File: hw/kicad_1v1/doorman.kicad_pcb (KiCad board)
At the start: 2 copper layers, 28 x 80 mm, 20 parts, among them J1 Ring Detection, J2 Lock, J3 Power Supply, K1 S1A05, Q1 BC337, U1 WeMos_mini, U2 PC817

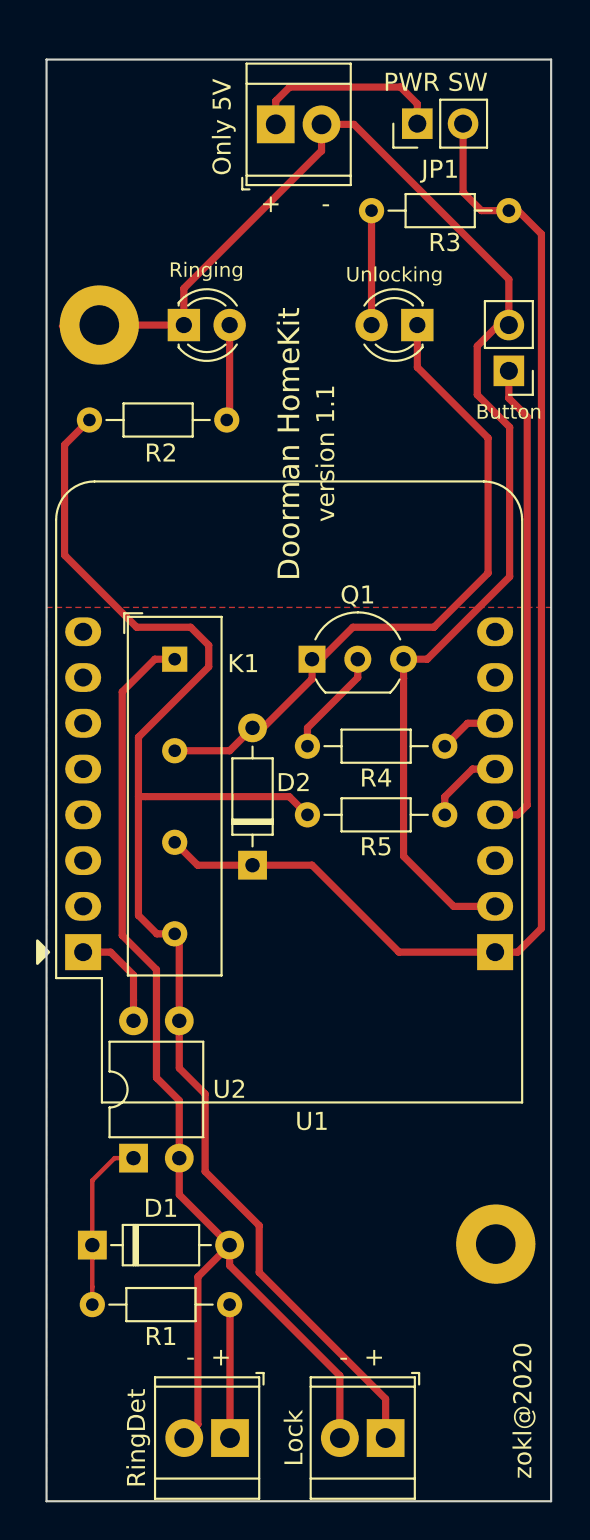
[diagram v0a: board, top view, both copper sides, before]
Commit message: Change description layout. Add cotas.
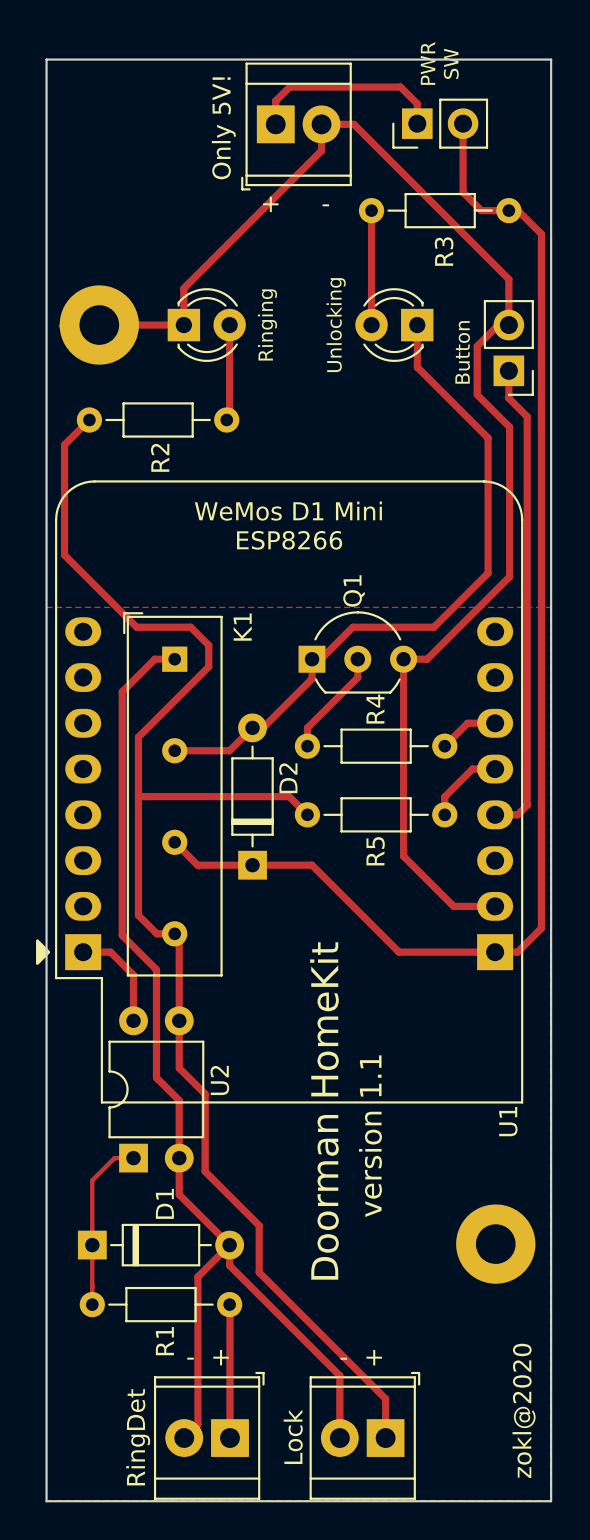
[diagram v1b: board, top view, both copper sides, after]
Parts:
-  : renamed from JP1
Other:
- board text added: "Only 5V!"
- board text added: "WeMos D1 Mini ESP8266"
- board text removed: "Only 5V"
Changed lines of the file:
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@@
   (general
     (thickness 1.6)
-    (drawings 21)
+    (drawings 24)
     (tracks 118)
     (zones 0)
@@
       (outputformat 4)
       (mirror false)
-      (drillshape 0)
+      (drillshape 2)
       (scaleselection 1)
       (outputdirectory "./"))
@@
     (descr "Through hole straight pin header, 1x02, 2.54mm pitch, single row")
     (tags "Through hole pin header THT 1x02 2.54mm single row")
-    (fp_text reference JP1 (at -2.54 1.27 180) (layer F.SilkS)
+    (fp_text reference " " (at 3.302 1.016 270) (layer F.SilkS)
       (effects (font (size 1 1) (thickness 0.15)))
     )
@@
     (descr "Diode, DO-35_SOD27 series, Axial, Horizontal, pin pitch=7.62mm, , length*diameter=4*2mm^2, , http://www.diodes.com/_files/packages/DO-35.pdf")
     (tags "Diode DO-35_SOD27 series Axial Horizontal pin pitch 7.62mm  length 4mm diameter 2mm")
-    (fp_text reference D1 (at 3.81 -2.032 -180) (layer F.SilkS)
+    (fp_text reference D1 (at 4.064 -2.286 90) (layer F.SilkS)
       (effects (font (size 1 1) (thickness 0.15)))
     )
@@
     (descr "4-lead though-hole mounted DIP package, row spacing 7.62 mm (300 mils)")
     (tags "THT DIP DIL PDIP 2.54mm 7.62mm 300mil")
-    (fp_text reference U2 (at 3.81 5.334 180) (layer F.SilkS)
+    (fp_text reference U2 (at 4.318 4.826 270) (layer F.SilkS)
       (effects (font (size 1 1) (thickness 0.15)))
     )
@@
     (descr "Resistor, Axial_DIN0204 series, Axial, Horizontal, pin pitch=7.62mm, 0.167W, length*diameter=3.6*1.6mm^2, http://cdn-reichelt.de/documents/datenblatt/B400/1_4W%23YAG.pdf")
     (tags "Resistor Axial_DIN0204 series Axial Horizontal pin pitch 7.62mm 0.167W length 3.6mm diameter 1.6mm")
-    (fp_text reference R5 (at 3.81 1.778) (layer F.SilkS)
+    (fp_text reference R5 (at 3.81 2.032 90) (layer F.SilkS)
       (effects (font (size 1 1) (thickness 0.15)))
     )
@@
     (descr "Diode, DO-35_SOD27 series, Axial, Horizontal, pin pitch=7.62mm, , length*diameter=4*2mm^2, , http://www.diodes.com/_files/packages/DO-35.pdf")
     (tags "Diode DO-35_SOD27 series Axial Horizontal pin pitch 7.62mm  length 4mm diameter 2mm")
-    (fp_text reference D2 (at 4.572 2.286 180) (layer F.SilkS)
+    (fp_text reference D2 (at 4.826 2.032 270) (layer F.SilkS)
       (effects (font (size 1 1) (thickness 0.15)))
     )
@@
     (descr "Resistor, Axial_DIN0204 series, Axial, Horizontal, pin pitch=7.62mm, 0.167W, length*diameter=3.6*1.6mm^2, http://cdn-reichelt.de/documents/datenblatt/B400/1_4W%23YAG.pdf")
     (tags "Resistor Axial_DIN0204 series Axial Horizontal pin pitch 7.62mm 0.167W length 3.6mm diameter 1.6mm")
-    (fp_text reference R4 (at 3.81 1.778) (layer F.SilkS)
+    (fp_text reference R4 (at 3.81 -2.032 90) (layer F.SilkS)
       (effects (font (size 1 1) (thickness 0.15)))
     )
@@
     (descr "16-pin module, column spacing 22.86 mm (900 mils), https://wiki.wemos.cc/products:d1:d1_mini, https://c1.staticflickr.com/1/734/31400410271_f278b087db_z.jpg")
     (tags "ESP8266 WiFi microcontroller")
-    (fp_text reference U1 (at 12.7 27.178) (layer F.SilkS)
+    (attr smd)
+    (fp_text reference U1 (at 23.622 27.178 90) (layer F.SilkS)
       (effects (font (size 1 1) (thickness 0.15)))
     )
@@
     (descr "TO-92 leads in-line, wide, drill 0.75mm (see NXP sot054_po.pdf)")
     (tags "to-92 sc-43 sc-43a sot54 PA33 transistor")
-    (fp_text reference Q1 (at 2.54 -3.556 180) (layer F.SilkS)
+    (fp_text reference Q1 (at 2.286 -3.81 270) (layer F.SilkS)
       (effects (font (size 1 1) (thickness 0.15)))
     )
@@
     (descr "Resistor, Axial_DIN0204 series, Axial, Horizontal, pin pitch=7.62mm, 0.167W, length*diameter=3.6*1.6mm^2, http://cdn-reichelt.de/documents/datenblatt/B400/1_4W%23YAG.pdf")
     (tags "Resistor Axial_DIN0204 series Axial Horizontal pin pitch 7.62mm 0.167W length 3.6mm diameter 1.6mm")
-    (fp_text reference R2 (at 3.65 -1.844) (layer F.SilkS)
+    (fp_text reference R2 (at 3.65 -2.098 90) (layer F.SilkS)
       (effects (font (size 1 1) (thickness 0.15)))
     )
@@
     (descr "Standex-Meder SIL-relais, Form 1A, see https://standexelectronics.com/wp-content/uploads/datasheet_reed_relay_SIL.pdf")
     (tags "Standex Meder SIL reed relais")
-    (fp_text reference K1 (at 0.254 -3.81 180) (layer F.SilkS)
+    (fp_text reference K1 (at -1.778 -3.81 270) (layer F.SilkS)
       (effects (font (size 1 1) (thickness 0.15)))
     )
@@
     (descr "Resistor, Axial_DIN0204 series, Axial, Horizontal, pin pitch=7.62mm, 0.167W, length*diameter=3.6*1.6mm^2, http://cdn-reichelt.de/documents/datenblatt/B400/1_4W%23YAG.pdf")
     (tags "Resistor Axial_DIN0204 series Axial Horizontal pin pitch 7.62mm 0.167W length 3.6mm diameter 1.6mm")
-    (fp_text reference R3 (at 4.064 1.778) (layer F.SilkS)
+    (fp_text reference R3 (at 4.064 2.286 90) (layer F.SilkS)
       (effects (font (size 1 1) (thickness 0.15)))
     )
@@
     (descr "Resistor, Axial_DIN0204 series, Axial, Horizontal, pin pitch=7.62mm, 0.167W, length*diameter=3.6*1.6mm^2, http://cdn-reichelt.de/documents/datenblatt/B400/1_4W%23YAG.pdf")
     (tags "Resistor Axial_DIN0204 series Axial Horizontal pin pitch 7.62mm 0.167W length 3.6mm diameter 1.6mm")
-    (fp_text reference R1 (at 3.81 -1.778 180) (layer F.SilkS)
+    (fp_text reference R1 (at 3.556 -2.032 270) (layer F.SilkS)
       (effects (font (size 1 1) (thickness 0.15)))
     )
@@
     (descr "Through hole straight pin header, 1x02, 2.54mm pitch, single row")
     (tags "Through hole pin header THT 1x02 2.54mm single row")
-    (fp_text reference Button (at 0 -2.286 180) (layer F.SilkS)
-      (effects (font (size 0.8 0.8) (thickness 0.2)))
+    (fp_text reference Button (at 2.54 1.016 270) (layer F.SilkS)
+      (effects (font (size 0.8 0.8) (thickness 0.15)))
     )
     (fp_text value Button (at 0 4.25) (layer F.Fab)
@@
     (descr "LED, diameter 3.0mm, 2 pins")
     (tags "LED diameter 3.0mm 2 pins")
-    (fp_text reference Unlocking (at 1.27 2.794 180) (layer F.SilkS)
+    (fp_text reference Unlocking (at 4.572 0 270) (layer F.SilkS)
       (effects (font (size 0.8 0.8) (thickness 0.15)))
     )
@@
     (descr "LED, diameter 3.0mm, 2 pins")
     (tags "LED diameter 3.0mm 2 pins")
-    (fp_text reference Ringing (at 1.25 -3.048 180) (layer F.SilkS)
+    (fp_text reference Ringing (at 4.572 0 270) (layer F.SilkS)
       (effects (font (size 0.8 0.8) (thickness 0.15)))
     )
@@
     )
   )
+  (dimension 83.000005 (width 0.12) (layer Margin)
+    (gr_text "83.000 mm" (at 136.872085 91.502313 90) (layer Margin)
+      (effects (font (size 1 1) (thickness 0.15)))
+    )
+    (feature1 (pts (xy 130.028 50) (xy 136.202505 50.002083)))
+    (feature2 (pts (xy 130 133) (xy 136.174505 133.002083)))
+    (crossbar (pts (xy 135.588085 133.001885) (xy 135.616085 50.001885)))
+    (arrow1a (pts (xy 135.616085 50.001885) (xy 136.202126 51.128587)))
+    (arrow1b (pts (xy 135.616085 50.001885) (xy 135.029284 51.128191)))
+    (arrow2a (pts (xy 135.588085 133.001885) (xy 136.174886 131.875579)))
+    (arrow2b (pts (xy 135.588085 133.001885) (xy 135.002044 131.875183)))
+  )
+  (dimension 30 (width 0.12) (layer Margin)
+    (gr_text "30.000 mm" (at 115 140.17) (layer Margin)
+      (effects (font (size 1 1) (thickness 0.15)))
+    )
+    (feature1 (pts (xy 130 133) (xy 130 139.486421)))
+    (feature2 (pts (xy 100 133) (xy 100 139.486421)))
+    (crossbar (pts (xy 100 138.9) (xy 130 138.9)))
+    (arrow1a (pts (xy 130 138.9) (xy 128.873496 139.486421)))
+    (arrow1b (pts (xy 130 138.9) (xy 128.873496 138.313579)))
+    (arrow2a (pts (xy 100 138.9) (xy 101.126504 139.486421)))
+    (arrow2b (pts (xy 100 138.9) (xy 101.126504 138.313579)))
+  )
+  (gr_text "WeMos D1 Mini\nESP8266" (at 114.534 77.178) (layer F.SilkS)
+    (effects (font (size 1 1) (thickness 0.15)))
+  )
   (gr_text "-  +" (at 110.072 123.27) (layer F.SilkS)
     (effects (font (size 1 1) (thickness 0.15)))
@@
   )
   (gr_line (start 130 133) (end 130 50) (layer Margin) (width 0.12))
-  (gr_text "PWR SW" (at 122.662 52.54) (layer F.SilkS)
-    (effects (font (size 1 1) (thickness 0.2)))
+  (gr_text "PWR\nSW" (at 122.916 51.524 90) (layer F.SilkS)
+    (effects (font (size 0.8 0.8) (thickness 0.15)))
   )
   (gr_line (start 129.072 131.27) (end 129.072 51.27) (layer Edge.Cuts) (width 0.12))
@@
     (effects (font (size 1 1) (thickness 0.15)))
   )
-  (gr_text "Only 5V" (at 110.822 55.02 90) (layer F.SilkS)
+  (gr_text "Only 5V!" (at 110.822 55.02 90) (layer F.SilkS)
     (effects (font (size 1 1) (thickness 0.2)))
   )
-  (gr_text "version 1.1" (at 116.566 73.114 90) (layer F.SilkS)
-    (effects (font (size 1 1) (thickness 0.2)))
-  )
-  (gr_text "Doorman HomeKit" (at 114.534 72.606 90) (layer F.SilkS)
-    (effects (font (size 1.2 1.2) (thickness 0.25)))
+  (gr_text "version 1.1" (at 119.106 110.96 90) (layer F.SilkS)
+    (effects (font (size 1.2 1.2) (thickness 0.2)))
+  )
+  (gr_text "Doorman HomeKit" (at 116.566 109.69 90) (layer F.SilkS)
+    (effects (font (size 1.5 1.5) (thickness 0.25)))
   )
   (gr_text zokl@2020 (at 127.508 126.238 90) (layer F.SilkS)
-    (effects (font (size 1 1) (thickness 0.2)))
+    (effects (font (size 1 1) (thickness 0.15)))
   )
   (gr_circle (center 127.5 52.5) (end 129 52.5) (layer Margin) (width 0.12))
